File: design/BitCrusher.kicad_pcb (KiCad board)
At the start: 2 copper layers, 181.5 x 86.2 mm, 138 parts, among them J1 BNC, J10 PJ-002BH, J2 BWSMA-KWE-Z001, J3 BWSMA-KE-Z001, J4 BWSMA-KE-Z001, J5 SHOU HAN TYPE-C 14P CC-2.6, J6 Conn_01x04_Pin, J7 Conn_01x04_Pin, J8 Conn_01x03_Pin, J9 Conn_01x03_Pin, Q1 SW4N60, Q2 2SA1213, Q3 GAN080-650EBE, T1 DA2033-AL, U1 STM32F303RETx, U2 USBLC6-2SC6, U3 FT230XQ, U4 TPS7A2050PDQN, U5 TPS7A2033PDQN, U6 LMR33630ADDA, U7 LMR33630ADDA, U8 TLP152TPL_E, U9 MAX22702EASA+

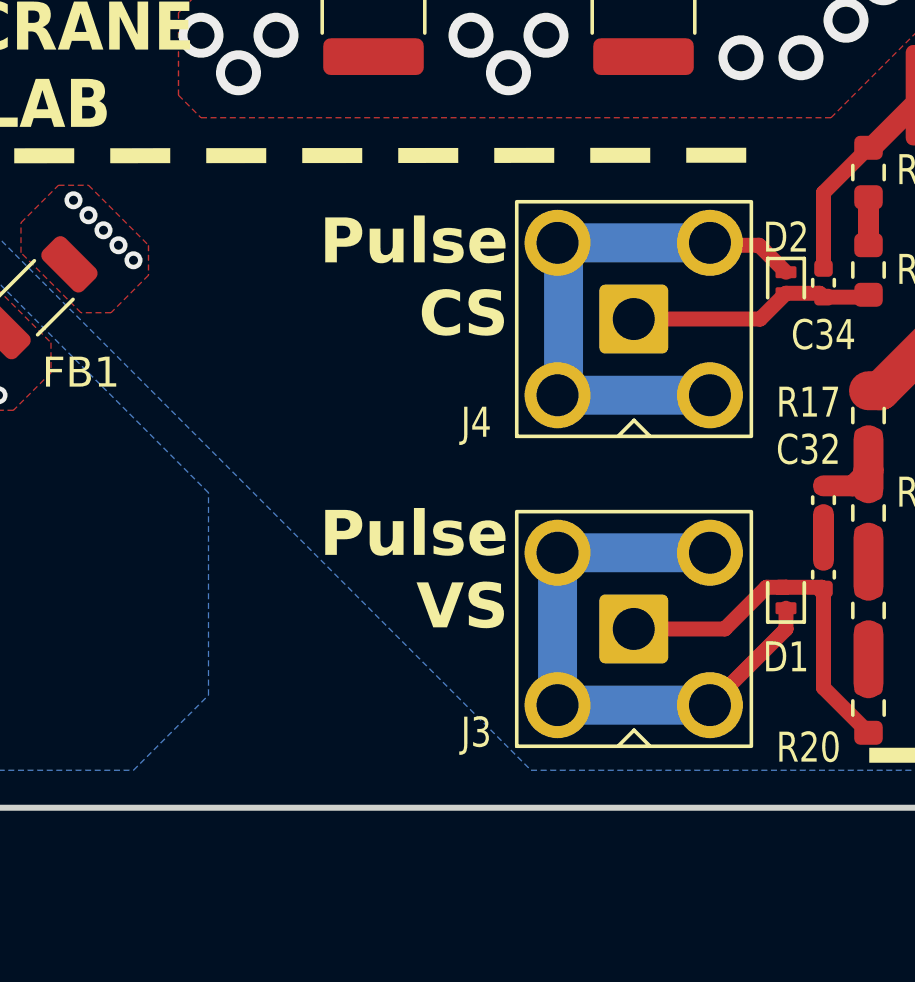
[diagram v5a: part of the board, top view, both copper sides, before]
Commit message: updated measurement buffer docs
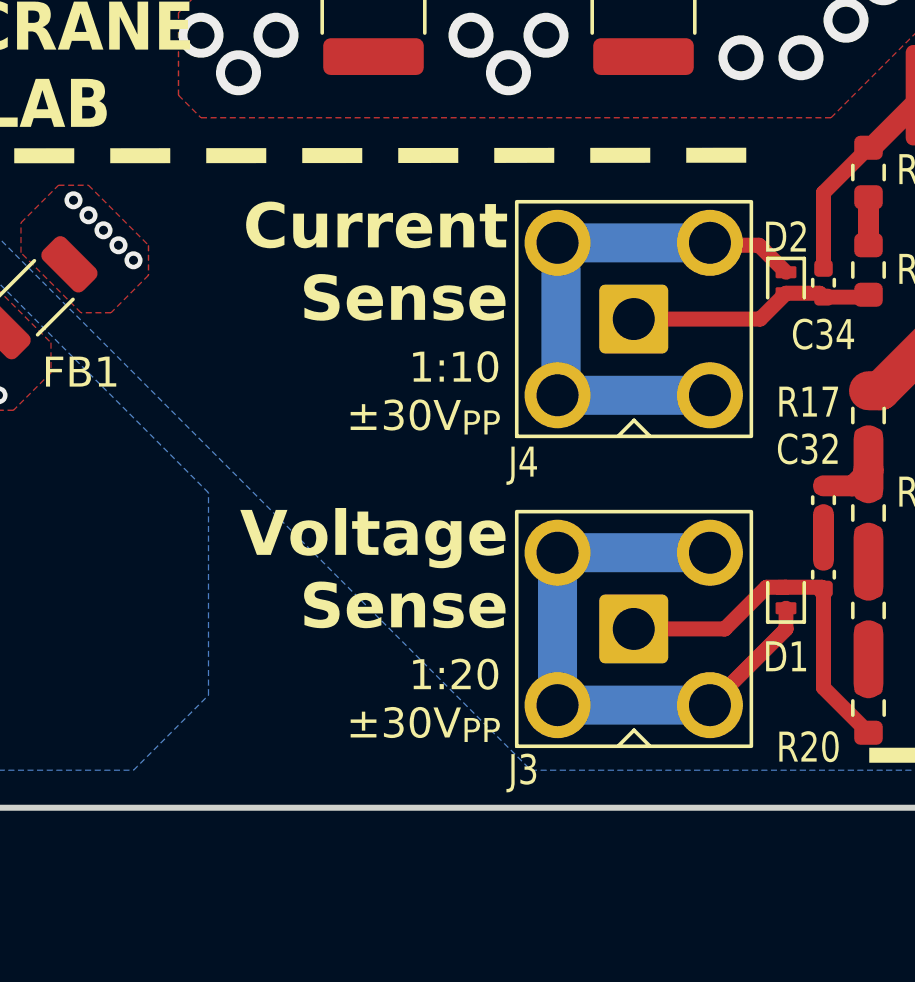
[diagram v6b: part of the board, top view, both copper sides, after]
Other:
- board text added: "1:10 ±30V_{PP}"
- board text added: "1:20 ±30V_{PP}"
- board text added: "Current Sense"
- board text added: "Voltage Sense"
- board text removed: "Pulse CS"
- board text removed: "Pulse VS"
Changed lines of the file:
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@@
 		(tags "SMA THT Female Jack Horizontal")
 		(property "Reference" "J3"
-			(at -3.46 -5.25 180)
+			(at -4.71 -3.675 180)
 			(layer "F.SilkS")
 			(effects
@@
 		(tags "SMA THT Female Jack Horizontal")
 		(property "Reference" "J4"
-			(at -3.46 -5.25 180)
+			(at -4.79 -3.675 180)
 			(layer "F.SilkS")
 			(effects
@@
 		)
 	)
+	(gr_text "1:10\n±30V_{PP}"
+		(at 212.75 108 0)
+		(layer "F.SilkS")
+		(effects
+			(font
+				(size 1 1)
+				(thickness 0.15)
+			)
+			(justify right top)
+		)
+	)
+	(gr_text "1:20\n±30V_{PP}"
+		(at 212.75 118.25 0)
+		(layer "F.SilkS")
+		(effects
+			(font
+				(size 1 1)
+				(thickness 0.15)
+			)
+			(justify right top)
+		)
+	)
 	(gr_text "DESIGNED BY GEORGE CRANE\nUNH, RESILIENT ARCH. LAB"
 		(at 169.25 100.75 0)
@@
 		)
 	)
-	(gr_text "Pulse\nCS"
-		(at 213 103.5 0)
+	(gr_text "Current\nSense"
+		(at 213 103 0)
 		(layer "F.SilkS")
 		(effects
@@
 		)
 	)
-	(gr_text "Pulse\nVS"
+	(gr_text "Voltage\nSense"
 		(at 213 113.25 0)
 		(layer "F.SilkS")
@@
 	)
 	(segment
-		(start 214.835 104.42)
-		(end 214.835 109.5)
+		(start 214.75 109.5)
+		(end 219.915 109.5)
 		(width 1.3)
 		(layer "B.Cu")
@@
 	)
 	(segment
-		(start 219.915 104.42)
-		(end 214.835 104.42)
-		(width 1.3)
+		(start 186.425 79.175)
+		(end 188 80.75)
+		(width 1)
 		(layer "B.Cu")
 		(net "PulseCS-")
 	)
 	(segment
-		(start 186.425 79.175)
-		(end 188 80.75)
-		(width 1)
+		(start 214.75 104.42)
+		(end 214.75 109.5)
+		(width 1.3)
 		(layer "B.Cu")
 		(net "PulseCS-")
@@
 	)
 	(segment
-		(start 214.635 119.83)
-		(end 219.715 119.83)
+		(start 219.915 104.42)
+		(end 214.75 104.42)
 		(width 1.3)
 		(layer "B.Cu")
@@
 	)
 	(segment
-		(start 214.835 109.5)
-		(end 219.915 109.5)
+		(start 214.635 119.83)
+		(end 219.715 119.83)
 		(width 1.3)
 		(layer "B.Cu")

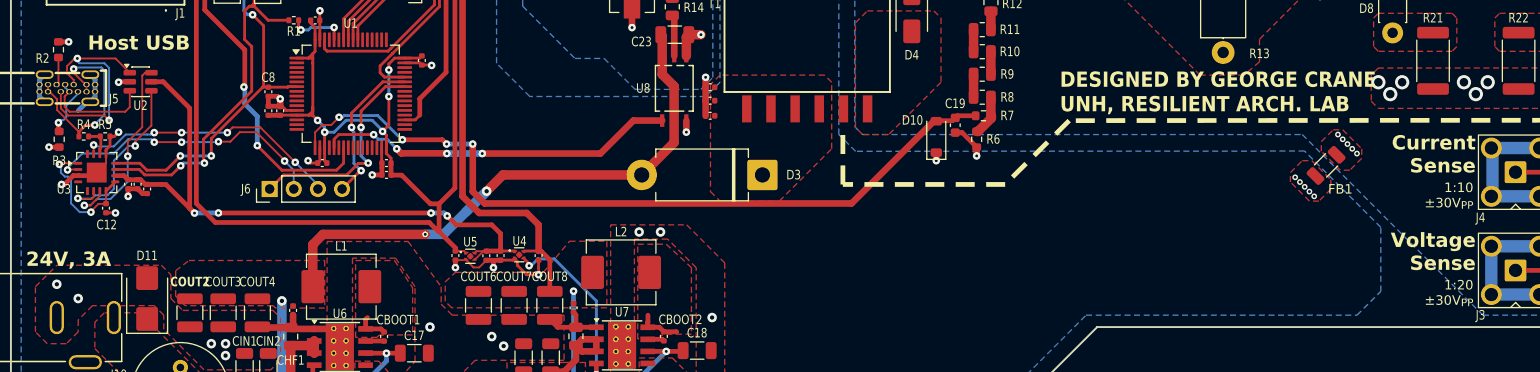
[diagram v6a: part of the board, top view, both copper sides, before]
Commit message: Reduced usage of 0.2mm traces (which don't fab well)
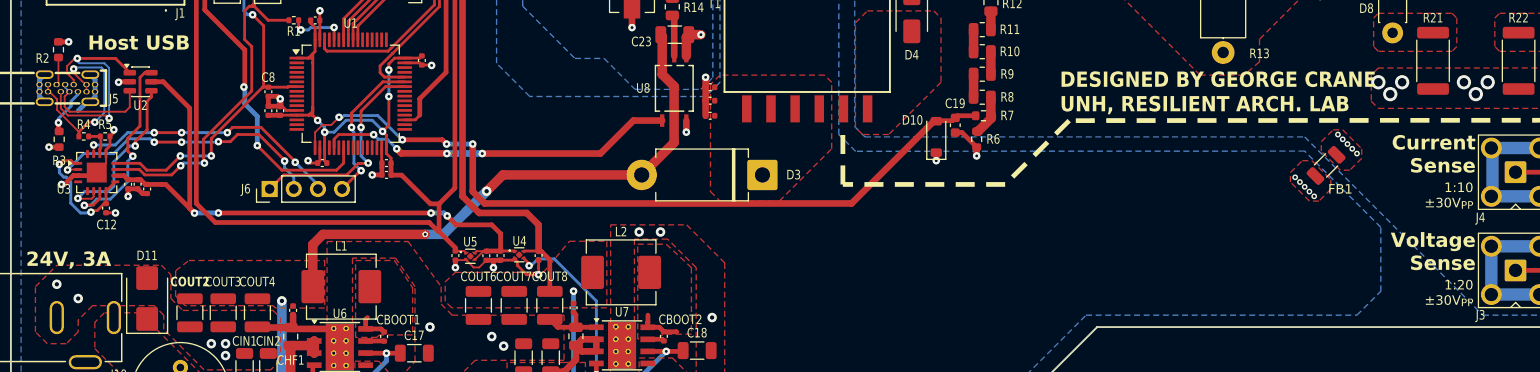
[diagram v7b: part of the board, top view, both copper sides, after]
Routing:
- net Net-(U3-USBDM): track 21.1 -> 21.7 mm
